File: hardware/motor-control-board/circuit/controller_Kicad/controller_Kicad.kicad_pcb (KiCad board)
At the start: 2 copper layers, 70 x 50 mm, 23 parts, among them CN1 2510-4AW, CN2 2510-4AW, SW1 SS-12D10L5

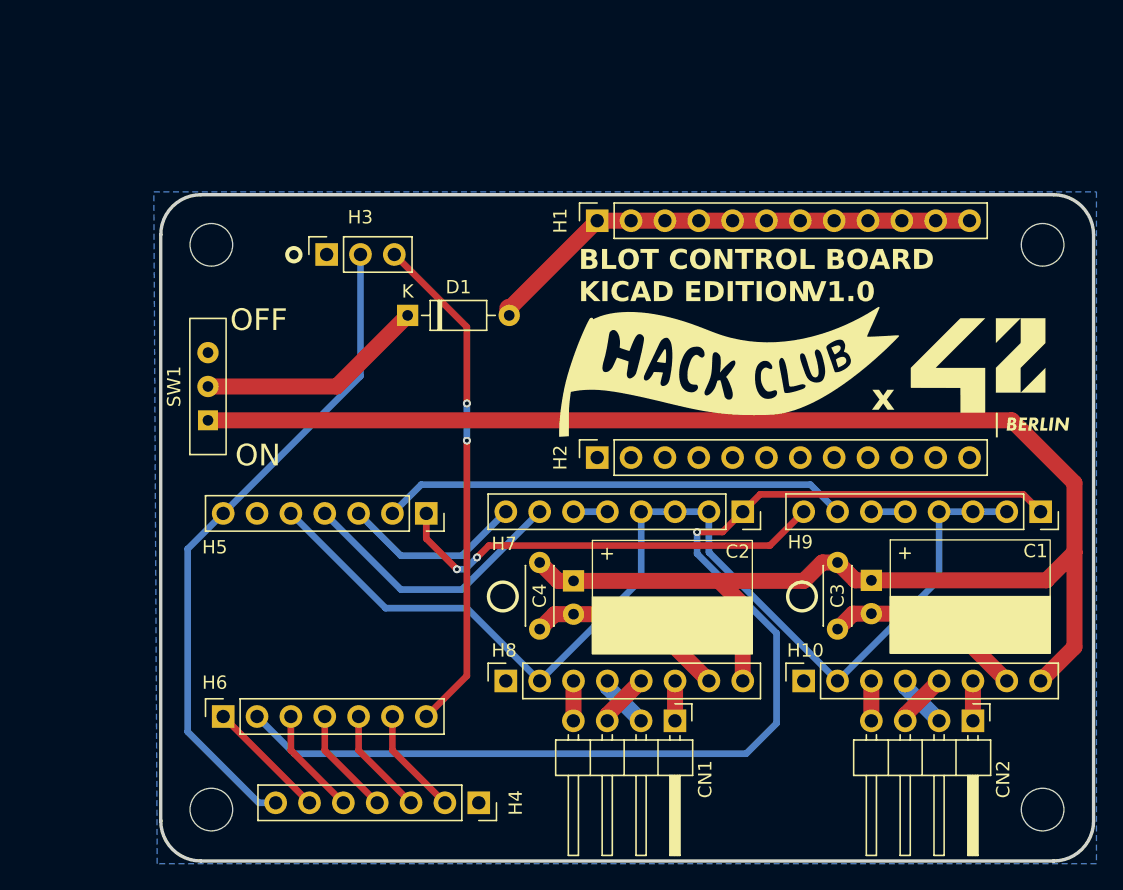
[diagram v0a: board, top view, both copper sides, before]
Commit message: re-laid out and re-routed PCB - V1.0 ready for production
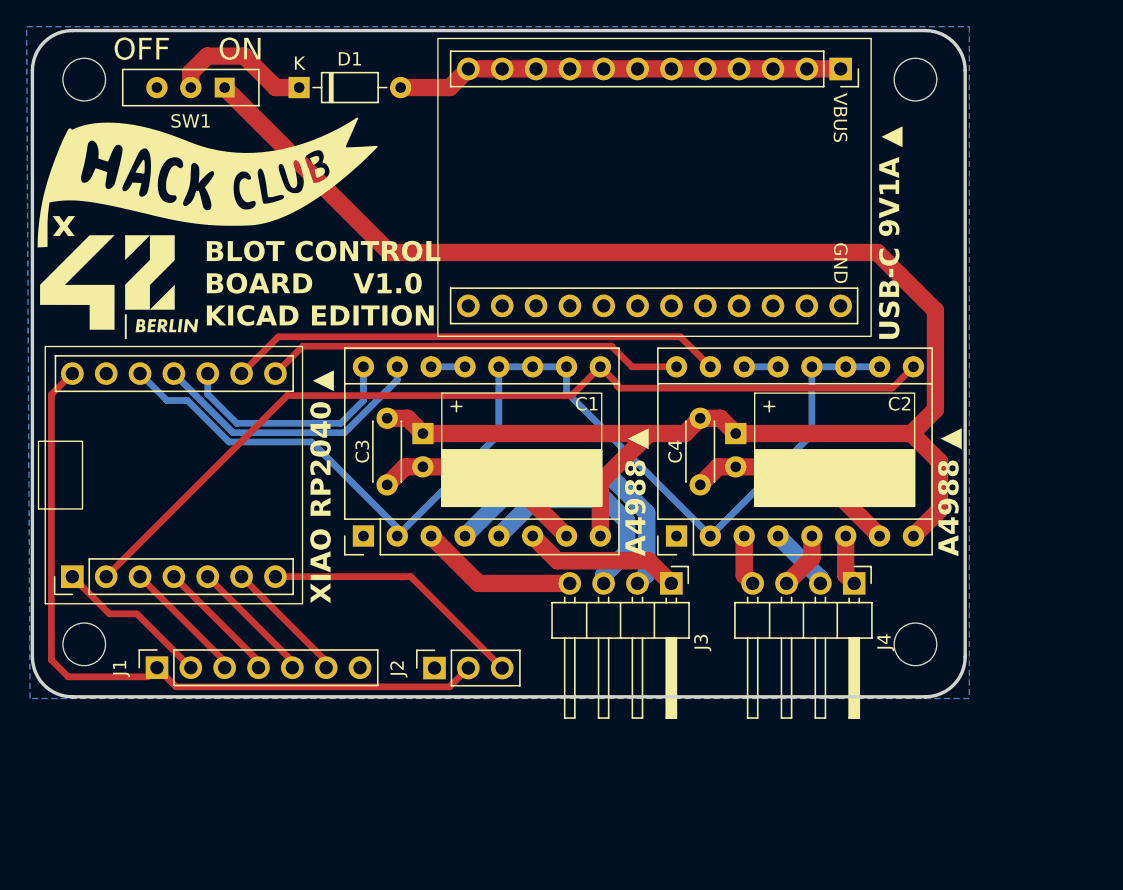
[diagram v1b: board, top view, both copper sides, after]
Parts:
- removed CN1, CN2: 2510-4AW, Connector_PinHeader_2.54mm:PinHeader_1x04_P2.54mm_Horizontal
- removed the G*** at (152.7, 93.3)
- removed H10, H7, H8, H9: PM254-1-08-Z-8.5, Connector_PinSocket_2.54mm:PinSocket_1x08_P2.54mm_Vertical
- removed H5, H6: PM254-1-07-Z-8.5, Connector_PinSocket_2.54mm:PinSocket_1x07_P2.54mm_Vertical
- removed PAD1, PAD2, PAD3, PAD4: HOLE3.2, Library:HOLE-3.2MM
- added G***: LOGO, Library:hcflag, F.Cu at (113.5, 79.1)
- added J1: Conn_01x07_Socket, Connector_PinSocket_2.54mm:PinSocket_1x07_P2.54mm_Vertical, F.Cu at (109.7, 115.5)
- added J2: Conn_01x03_Socket, Connector_PinSocket_2.54mm:PinSocket_1x03_P2.54mm_Vertical, F.Cu at (130.6, 115.6)
- added J3: Conn_01x04_Socket, Connector_PinHeader_2.54mm:PinHeader_1x04_P2.54mm_Horizontal, F.Cu at (148.3, 109.2)
- added J4: Conn_01x04_Socket, Connector_PinHeader_2.54mm:PinHeader_1x04_P2.54mm_Horizontal, F.Cu at (162.1, 109.2)
- added U1: USB-C_POWER_BOARD_9V_1A, Library:USB-C_POWER_BOARD_9V_1A, F.Cu at (147.1, 79.5)
- added U2: XIAO_RP2040_SEEED, Library:XIAO_RP2040_SEEED, F.Cu at (111.0, 108.7)
- added U3: Pololu_Breakout_A4988, Module:Pololu_Breakout-16_15.2x20.3mm, F.Cu at (125.2, 105.7)
- added U4: Pololu_Breakout_A4988, Module:Pololu_Breakout-16_15.2x20.3mm, F.Cu at (148.7, 105.7)
- D1: value 1N5819 -> D
- H1, H2: value KH-2.54FH-1X12P-H8.5 -> MountingHole 3.2mm; footprint Connector_PinSocket_2.54mm:PinSocket_1x12_P2.54mm_Vertical -> Library:HOLE-3.2MM
- H3: value Header-Male-2.54_1x3 -> MountingHole 3.2mm; footprint Connector_PinSocket_2.54mm:PinSocket_1x03_P2.54mm_Vertical -> Library:HOLE-3.2MM
- H4: value PM254-1-07-Z-8.5 -> MountingHole 3.2mm; footprint Connector_PinSocket_2.54mm:PinSocket_1x07_P2.54mm_Vertical -> Library:HOLE-3.2MM
- SW1: value SS-12D10L5 -> Slideswitch
- moved H3 46.1 mm to (166.7, 71.4), turned to 0 degrees
- moved H2 41.0 mm to (104.3, 113.8), turned to 0 degrees
- moved H1 39.9 mm to (104.3, 71.4), turned to 0 degrees
- moved C3 35.5 mm to (127.0, 96.8)
- moved C1 35.4 mm to (129.7, 100.4)
- moved H4 34.9 mm to (166.7, 113.8), turned to 0 degrees
- moved SW1 22.5 mm to (112.3, 72.0), turned to 180 degrees
- moved D1 18.9 mm to (120.4, 72.0)
- moved C2 16.4 mm to (153.2, 100.4)
- moved C4 16.2 mm to (150.5, 96.8)
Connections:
- D1 pad 2: Net-(D1-Pad2) -> Net-(D1-A)
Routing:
- net Net-(D1-Pad2): track 37.8 -> 0.00 mm
- net Net-(D1-A): track 0.00 -> 33.6 mm
- net A6: track 38.2 -> 19.9 mm, vias 2 -> 0
- net U3-1A: track 4.17 -> 22.0 mm
- net ENABLE: track 85.4 -> 68.5 mm, vias 1 -> 0
- net U3-2A: track 4.04 -> 16.8 mm
- net U3-2B: track 2.99 -> 11.9 mm
- net U3-1B: track 3.16 -> 11.9 mm
- net Net-(D1-K): track 17.2 -> 10.7 mm
- net +5V: track 50.0 -> 55.4 mm
- net U4-1A: track 0.00 -> 4.87 mm
- net U4-2A: track 0.00 -> 4.35 mm
- net +9V: track 133.8 -> 129.6 mm
- net U2-1A: track 4.17 -> 0.00 mm
- net U2-2A: track 4.06 -> 0.00 mm
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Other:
- board text added: "A4988 ▲"
- board text added: "USB-C 9V1A ▲"
- board text added: "XIAO RP2040 ▲"
